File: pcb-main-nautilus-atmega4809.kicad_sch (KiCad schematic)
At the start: 11 parts, among them J1 694106301002, J2 105017-0001, J3 FTSH-105-01-L-DV-007-K, J4 75844-101-06LF, J5 66951-006LF, J6 66951-010LF, J7 66951-008LF, J8 66951-008LF

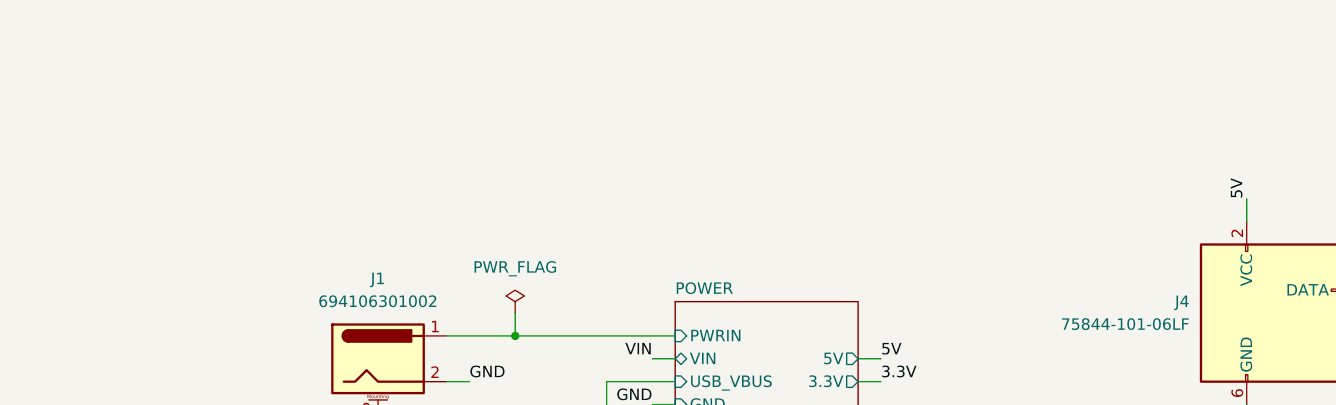
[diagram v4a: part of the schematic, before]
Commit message: Add sheet decoder
Supports #2.
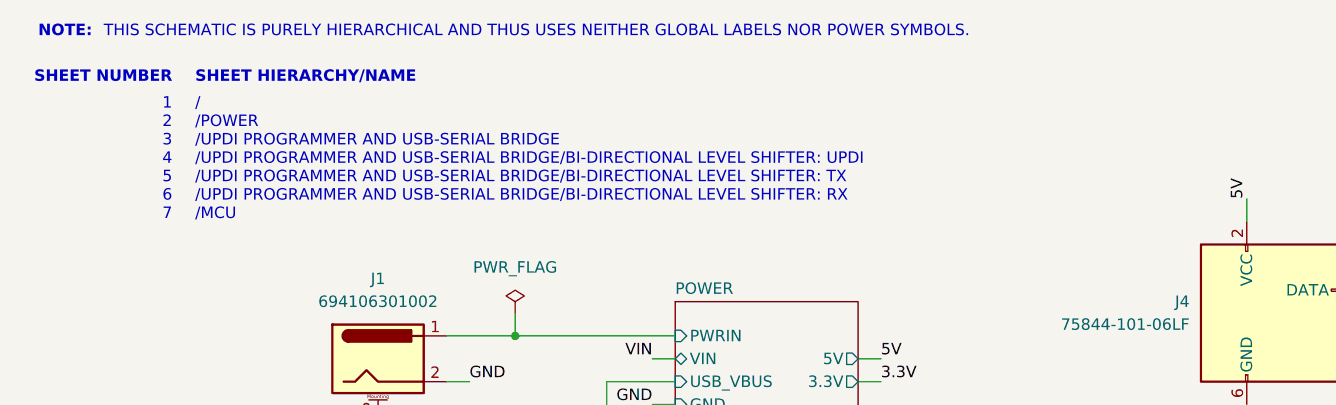
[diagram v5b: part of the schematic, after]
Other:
- note added: "/ /POWER /UPDI PROGRAMMER AND USB-SERIAL BRIDGE /UPDI PROGRAMMER AND USB-SERIAL BRIDGE/BI-DIRECTIONAL LEVEL SHIFTER: UPDI /UPDI PROGRAMMER AND USB-SERIAL BRIDGE/BI-DIRECTIONAL LEVEL SHIFTER: TX /UPDI PROGRAMMER AND USB-SERIAL BRIDGE/BI-DIRECTIONAL LEVEL SHIFTER: RX /MCU"
- note added: "1 2 3 4 5 6 7"
- note added: "NOTE:"
- note added: "SHEET HIERARCHY/NAME"
- note added: "SHEET NUMBER"
- note added: "THIS SCHEMATIC IS PURELY HIERARCHICAL AND THUS USES NEITHER GLOBAL LABELS NOR POWER SYMBOLS."
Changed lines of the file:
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@@
     (stroke (width 0) (type default) (color 0 0 0 0))
+  )
+  (text "/\n/POWER\n/UPDI PROGRAMMER AND USB-SERIAL BRIDGE\n/UPDI PROGRAMMER AND USB-SERIAL BRIDGE/BI-DIRECTIONAL LEVEL SHIFTER: UPDI\n/UPDI PROGRAMMER AND USB-SERIAL BRIDGE/BI-DIRECTIONAL LEVEL SHIFTER: TX\n/UPDI PROGRAMMER AND USB-SERIAL BRIDGE/BI-DIRECTIONAL LEVEL SHIFTER: RX\n/MCU"
+    (at 35.56 40.64 0)
+    (effects (font (size 1.27 1.27)) (justify left bottom))
+  )
+  (text "SHEET HIERARCHY/NAME" (at 35.56 25.4 0)
+    (effects (font (size 1.27 1.27) (thickness 0.254) bold) (justify left bottom))
+  )
+  (text "1\n2\n3\n4\n5\n6\n7" (at 33.02 40.64 180)
+    (effects (font (size 1.27 1.27)) (justify right bottom))
+  )
+  (text "THIS SCHEMATIC IS PURELY HIERARCHICAL AND THUS USES NEITHER GLOBAL LABELS NOR POWER SYMBOLS."
+    (at 25.4 20.32 0)
+    (effects (font (size 1.27 1.27)) (justify left bottom))
+  )
+  (text "SHEET NUMBER" (at 33.02 25.4 180)
+    (effects (font (size 1.27 1.27) bold) (justify right bottom))
+  )
+  (text "NOTE:" (at 24.13 20.32 180)
+    (effects (font (size 1.27 1.27) (thickness 0.254) bold) (justify right bottom))
   )
   (label "GND" (at 152.4 63.5 270)
